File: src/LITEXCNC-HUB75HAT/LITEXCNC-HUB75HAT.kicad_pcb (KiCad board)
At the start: 2 copper layers, 143.5 x 91.4 mm, 114 parts, among them J1 Conn_02x13_Odd_Even, J10 Conn_01x02, J11 HUB75, J12 HUB75, J13 V7.0, J14 V8.0, J15 HUB75, J16 HUB75, J17 Conn_02x20_Odd_Even, J2 Conn_02x13_Odd_Even, J3 Conn_02x13_Odd_Even, J4 HUB75, J5 HUB75, J6 HUB75, J7 v7.0, J8 v8.0, J9 HUB75, U1 74CB3T3245, U10 MAX3485, U11 74HC04, U12 MAX3485, U2 74CB3T3245, U3 74CB3T3245, U4 74CB3T3245, U5 74CB3T3245, U6 74CB3T3245, U8 74CB3T3245, U9 74HC04

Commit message: Version 1.1
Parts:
- removed C8: 100n, Capacitor_SMD:C_1206_3216Metric_Pad1.33x1.80mm_HandSolder
- added U7: 74HC04, Package_SO:SOIC-14_3.9x8.7mm_P1.27mm, B.Cu at (161.7, -81.8)
- C1, C11, C13, C17, C18, C2, C3, C4, C5, C6: value 0.1uF -> 100nF; moved to B.Cu
- C10, C15: footprint Capacitor_SMD:C_1206_3216Metric_Pad1.33x1.80mm_HandSolder -> Capacitor_SMD:C_0603_1608Metric_Pad1.08x0.95mm_HandSolder
- C12, C14, R11, R21, R3, R4, R5, U10, U11, U12, U8, U9: moved to B.Cu
- C16, C19, C20, C21, C9: value 0.1uF -> 100nF
- C7: value 1u -> 100nF; moved to B.Cu
- J1, J2, J3: footprint Connector_PinHeader_2.54mm:PinHeader_2x13_P2.54mm_Vertical -> Connector_IDC:IDC-Header_2x13_P2.54mm_Vertical
- R1: footprint Resistor_SMD:R_1206_3216Metric_Pad1.30x1.75mm_HandSolder -> Resistor_SMD:R_0805_2012Metric_Pad1.20x1.40mm_HandSolder; moved to B.Cu
- R10, R18, R19, R20, R7, R9: value 4.6K -> 4.7K; moved to B.Cu
- R12, R13, R14, R15: value 2.4k -> 150; footprint Resistor_SMD:R_1206_3216Metric_Pad1.30x1.75mm_HandSolder -> Resistor_SMD:R_0805_2012Metric_Pad1.20x1.40mm_HandSolder; moved to B.Cu
- R16, R6: value 4.6k -> 4.7k; moved to B.Cu
- R17, R8: footprint Resistor_SMD:R_1206_3216Metric_Pad1.30x1.75mm_HandSolder -> Resistor_SMD:R_0603_1608Metric_Pad0.98x0.95mm_HandSolder
- R2: value 140 -> 150; footprint Resistor_SMD:R_1206_3216Metric_Pad1.30x1.75mm_HandSolder -> Resistor_SMD:R_0805_2012Metric_Pad1.20x1.40mm_HandSolder; moved to B.Cu
- RN1, RN10, RN11, RN12, RN2, RN3, RN4, RN5, RN6, RN7, RN8, RN9: value 3.3k -> CN1J4KTTD1002F; footprint Resistor_SMD:R_Array_Convex_4x1206 -> Resistor_SMD:R_Array_Convex_4x0603_handsolder; moved to B.Cu
- moved C7 25.4 mm to (167.6, -82.7)
- moved R12 21.7 mm to (197.2, -98.5)
- moved R13 21.7 mm to (197.2, -96.1)
- moved R1 21.3 mm to (156.7, -69.5)
- moved C10 21.2 mm to (187.3, -92.2)
- moved C14 20.6 mm to (212.1, -51.0), turned to 0 degrees
- moved R2 20.5 mm to (159.1, -69.5)
- moved R8 20.2 mm to (185.8, -92.1)
- moved D4 19.7 mm to (183.8, -91.4)
- moved C11 17.2 mm to (182.8, -95.5)
- moved R20 15.7 mm to (219.3, -63.8), turned to 90 degrees
- moved J17 14.5 mm to (212.9, -70.7)
- moved R10 14.3 mm to (206.9, -93.8)
- moved R21 14.1 mm to (217.8, -59.9), turned to 180 degrees
- moved R4 13.8 mm to (252.9, -100.6)
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- renumbered RX to D6, TX to D7, RX to D8, TX to D9, RS489-1 to RS485-1, RS489-5 to RS485-5
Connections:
- C7 pad 1: GND -> +3.3V
- C7 pad 2: VDD -> GND
- J13 pad 2: VDD -> unconnected-(J13-Pin_2-Pad2)
- J14 pad 2: VDD -> unconnected-(J14-Pin_2-Pad2)
- J16 pad 11: ENA -> ENA_IN
- U8 pad 11: unconnected-(U8-B7-Pad11) -> PORTA1
- U8 pad 12: unconnected-(U8-B6-Pad12) -> PORTB1
- U8 pad 13: unconnected-(U8-B5-Pad13) -> PORTC1
- U8 pad 15: PORTC1 -> unconnected-(U8-B3-Pad15)
- U8 pad 16: PORTB1 -> unconnected-(U8-B2-Pad16)
- U8 pad 17: PORTA1 -> unconnected-(U8-B1-Pad17)
- U8 pad 18: ENA-LED -> unconnected-(U8-B0-Pad18)
- U8 pad 2: ENA -> unconnected-(U8-A0-Pad2)
- U8 pad 3: J4:7 -> unconnected-(U8-A1-Pad3)
- U8 pad 4: J4:8 -> unconnected-(U8-A2-Pad4)
- U8 pad 5: J4:9 -> unconnected-(U8-A3-Pad5)
- U8 pad 7: unconnected-(U8-A5-Pad7) -> J4:9
- U8 pad 8: unconnected-(U8-A6-Pad8) -> J4:8
- U8 pad 9: unconnected-(U8-A7-Pad9) -> J4:7
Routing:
- net ENA: track 305.6 -> 239.2 mm, vias 5 -> 6
- net +3.3V: track 346.6 -> 404.5 mm, vias 12 -> 13
- net ENA-LED: track 66.1 -> 8.25 mm
- net ENA_IN: track 0.00 -> 56.8 mm
- net +5V: track 401.6 -> 353.7 mm
- net Net-(R12-Pad1): track 28.4 -> 4.98 mm, vias 2 -> 0
- net /JTAG.TMS: track 68.3 -> 45.1 mm
- net J4:9: track 75.0 -> 51.8 mm, vias 1 -> 0
- net Net-(R13-Pad1): track 29.1 -> 6.20 mm, vias 2 -> 0
- net Net-(D1-A): track 5.09 -> 27.9 mm, vias 0 -> 1
- net TXD1: track 39.1 -> 16.6 mm, vias 0 -> 1
- net Net-(R15-Pad1): track 27.9 -> 6.20 mm
- net Net-(D6-A): track 3.73 -> 25.3 mm, vias 0 -> 1
- net J4:7: track 71.7 -> 50.2 mm, vias 1 -> 0
- net Net-(D7-A): track 3.73 -> 25.3 mm, vias 0 -> 1
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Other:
- board text added: "+"
- board text added: "R4"
- board text added: "V1.1"
- board text removed: "V1.0"

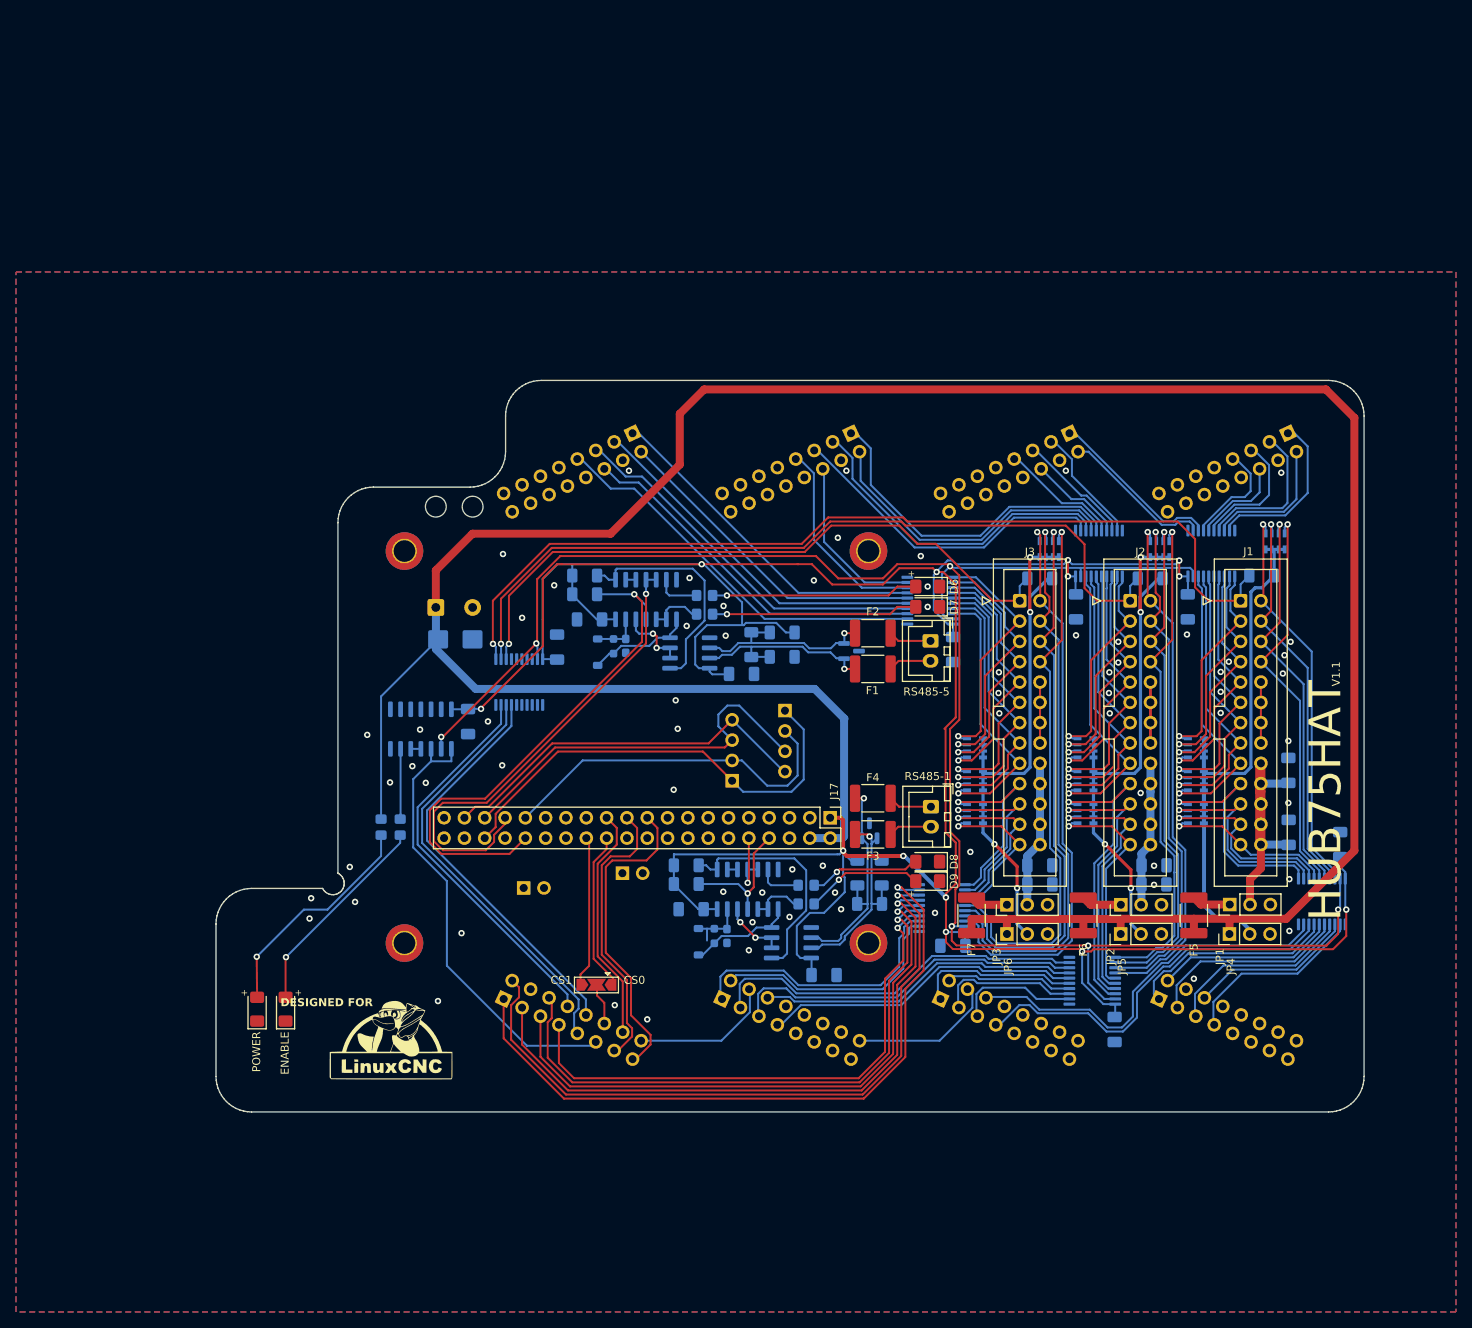
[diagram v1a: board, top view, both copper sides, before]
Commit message: Updated labels
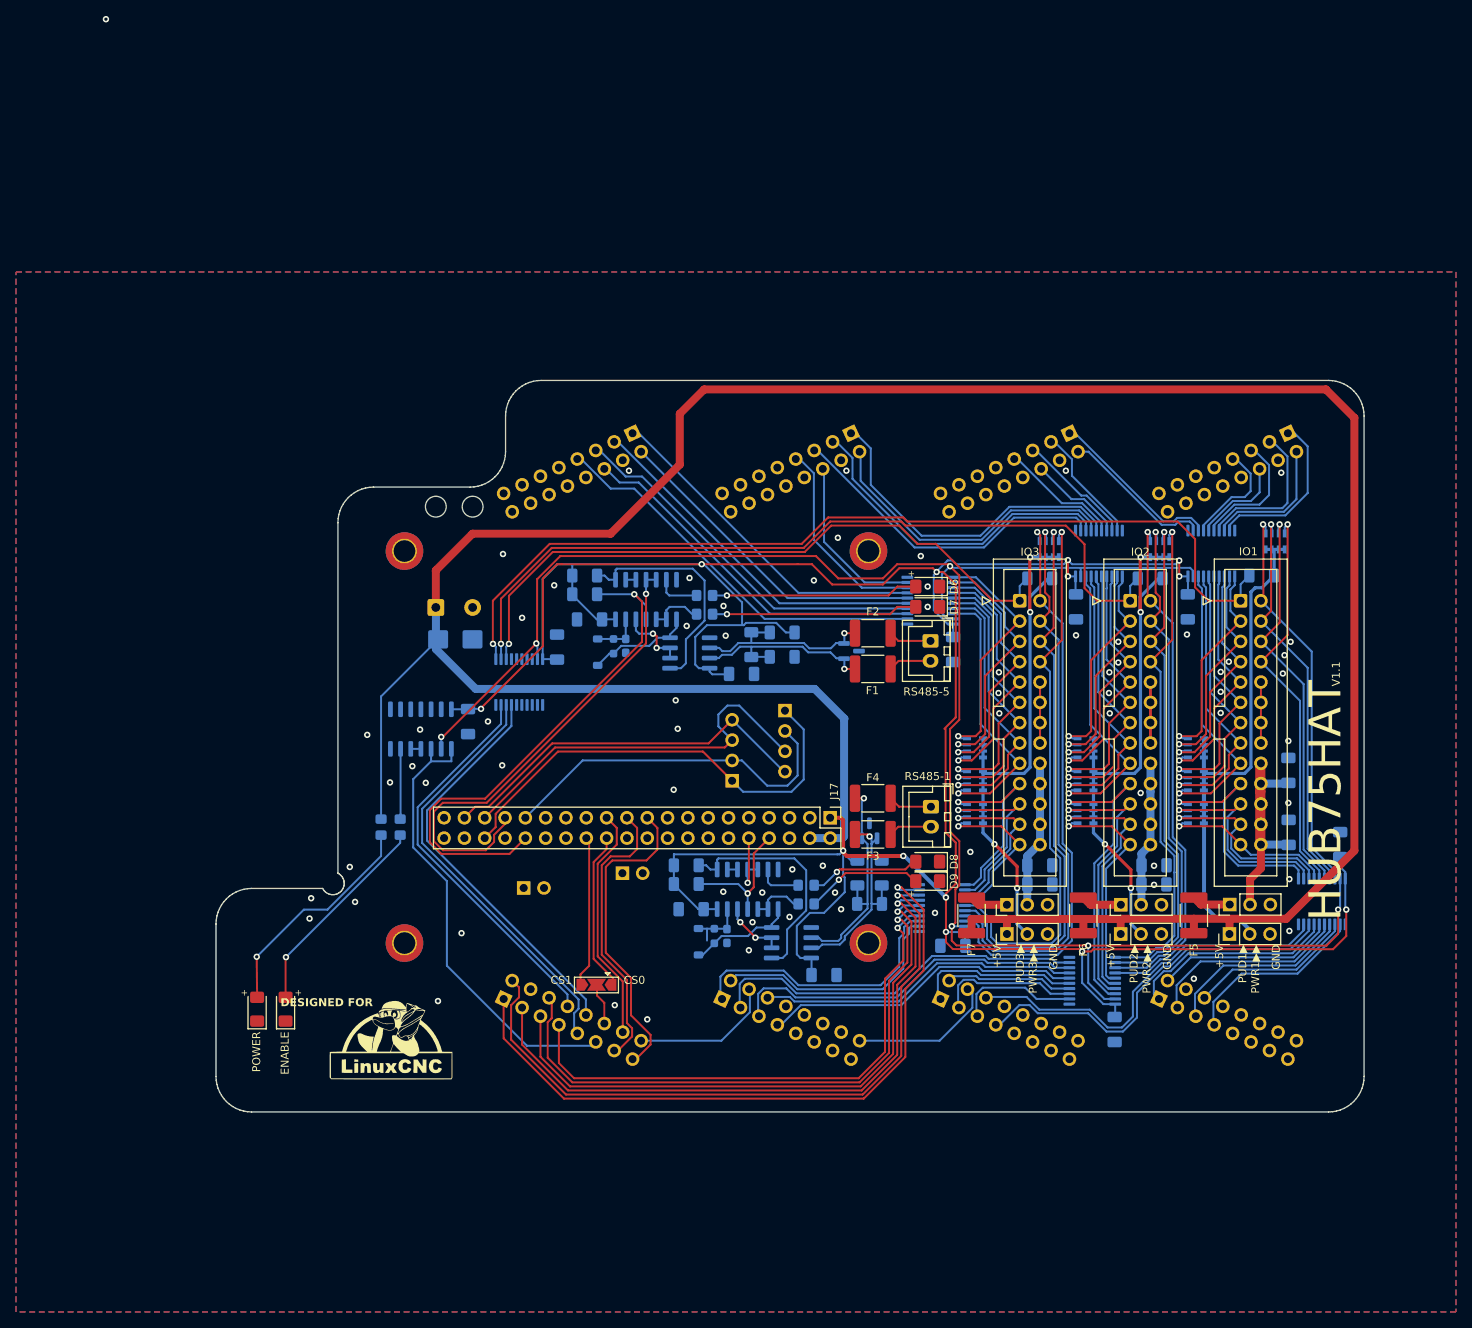
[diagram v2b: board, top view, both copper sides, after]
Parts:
- renumbered J1 to IO1, J2 to IO2, J3 to IO3
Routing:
- net (no net): vias 0 -> 1
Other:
- board text added: "+5V"
- board text added: "GND"
- board text added: "PUD1▶ PWR1▶▶"
- board text added: "PUD2▶ PWR2▶▶"
- board text added: "PUD3▶ PWR3▶▶"
